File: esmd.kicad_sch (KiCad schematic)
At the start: 21 parts, among them J1 Conn_01x04, J2 Conn_01x08, J3 Conn_01x04, J4 Conn_01x08, J5 Conn_01x04, J6 Conn_01x08, J7 Conn_01x02, J8 Conn_01x02, U1 74HC245, U2 74HC245, U3 LM78M05_TO252

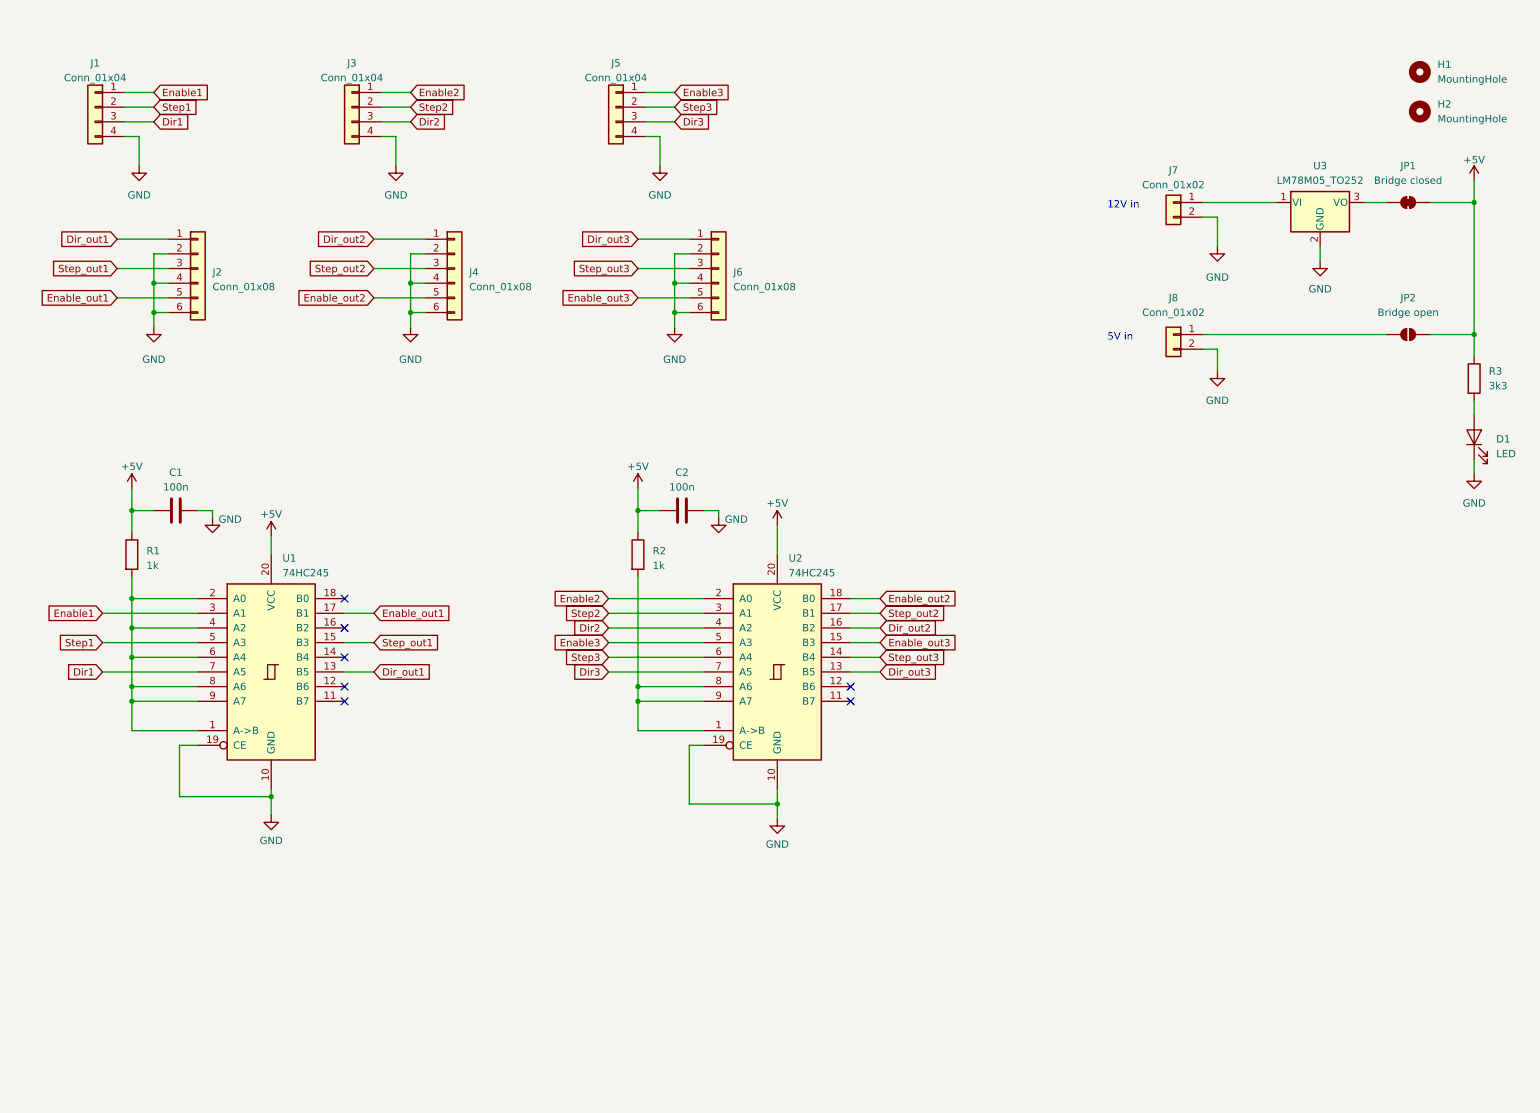
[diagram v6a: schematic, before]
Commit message: Add alternate footprints.
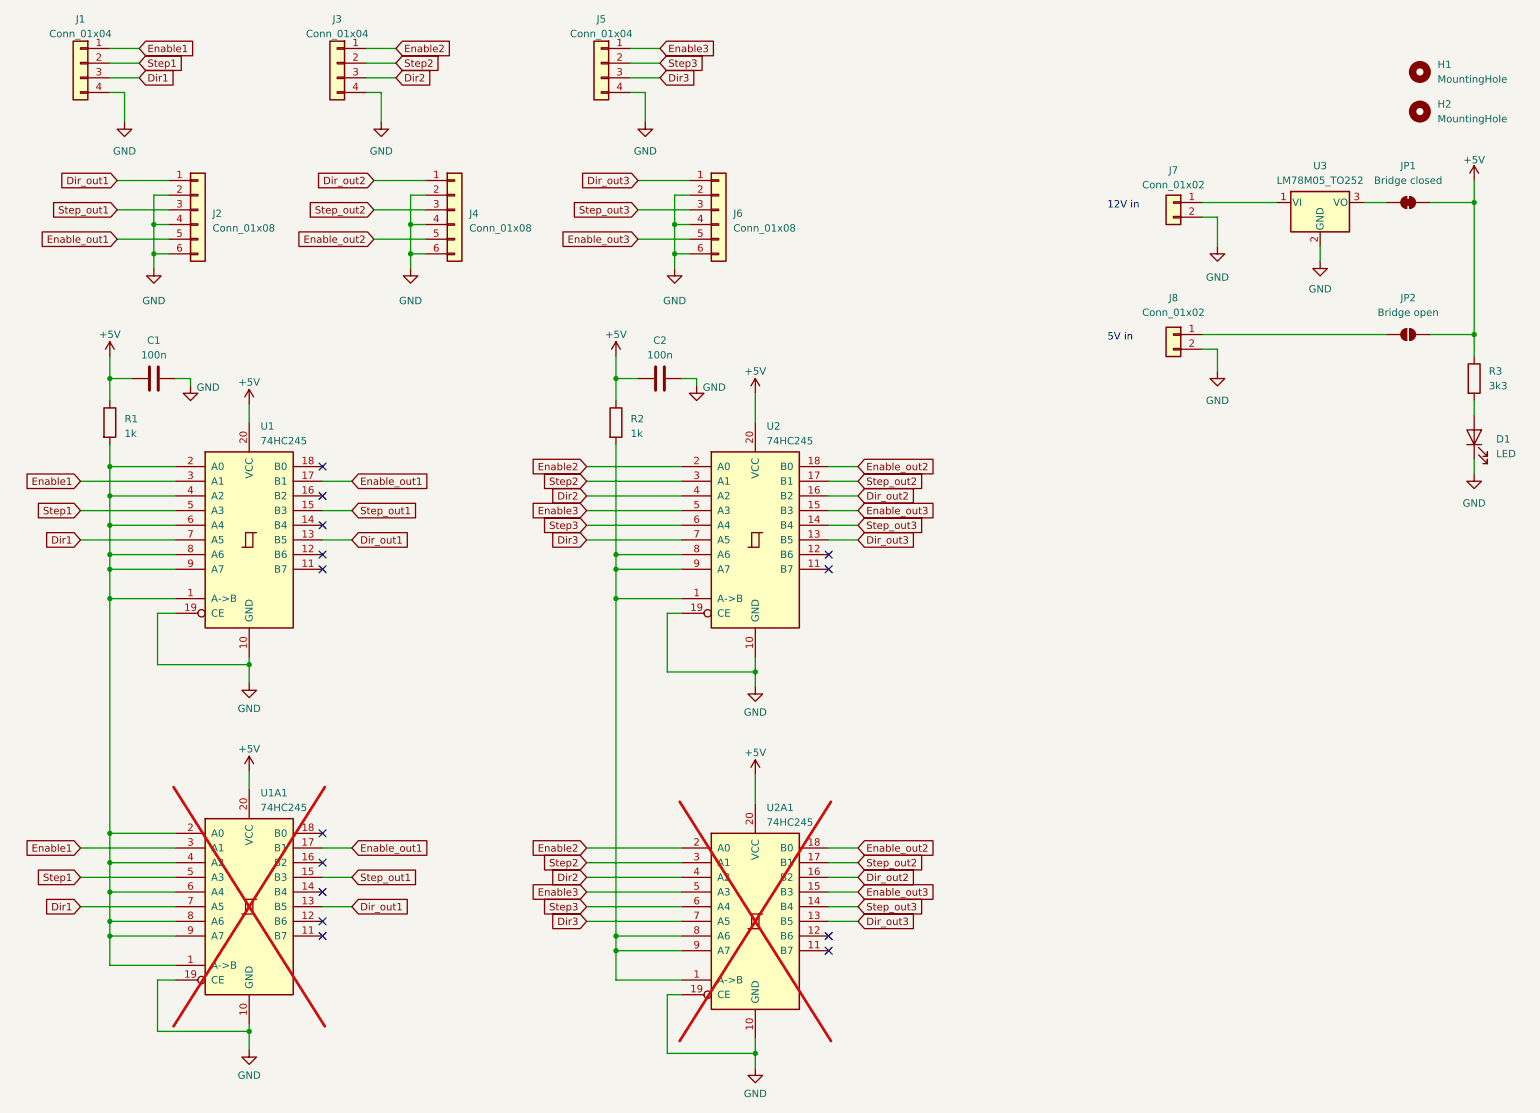
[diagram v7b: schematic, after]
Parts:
- added U1A1, U2A1: 74HC245, Package_SO:SOP-20_7.5x12.8mm_P1.27mm, symbol 74xx:74HC245
- U1, U2: footprint Package_SO:SO-20_5.3x12.6mm_P1.27mm -> PCM_Package_SO_AKL:SO-20_5.3x12.6mm_P1.27mm
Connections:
- net +5V: now also U1A1.20 (VCC), U2A1.20 (VCC)
- net Dir1: now also U1A1.7 (A5)
- net Dir2: now also U2A1.4 (A2)
- net Dir3: now also U2A1.7 (A5)
- net Dir_out1: now also U1A1.13 (B5)
- net Dir_out2: now also U2A1.16 (B2)
- net Dir_out3: now also U2A1.13 (B5)
- net Enable1: now also U1A1.3 (A1)
- net Enable2: now also U2A1.2 (A0)
- net Enable3: now also U2A1.5 (A3)
- net Enable_out1: now also U1A1.17 (B1)
- net Enable_out2: now also U2A1.18 (B0)
- net Enable_out3: now also U2A1.15 (B3)
- net GND: now also U1A1.10 (GND), U1A1.19 (CE), U2A1.10 (GND), U2A1.19 (CE)
- net Step1: now also U1A1.5 (A3)
- net Step2: now also U2A1.3 (A1)
- net Step3: now also U2A1.6 (A4)
- net Step_out1: now also U1A1.15 (B3)
- net Step_out2: now also U2A1.17 (B1)
- net Step_out3: now also U2A1.14 (B4)
- net at R2.2, U2.1 (A->B), U2.8 (A6)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: now also U2A1.1 (A->B), U2A1.8 (A6), U2A1.9 (A7)
- net at R1.2, U1.1 (A->B), U1.2 (A0)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: now also U1A1.1 (A->B), U1A1.2 (A0), U1A1.4 (A2), U1A1.6 (A4), U1A1.8 (A6), U1A1.9 (A7)
- no-connect marks 7 -> 14
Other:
- moved on the sheet: C1, C2, J1, J2, J3, J4, J5, J6, R1, R2, U1, U2
